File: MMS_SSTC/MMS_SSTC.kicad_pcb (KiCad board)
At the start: 2 copper layers, 80 x 80 mm, 39 parts, among them J1 Screw_Terminal_01x02, J2 Screw_Terminal_01x02, Q1 FQA8N100C, U1 NE555P, U2 UCC37322P, U3 LM7812_TO220, U4 LM7805_TO220, Y1 CXO_DIP8

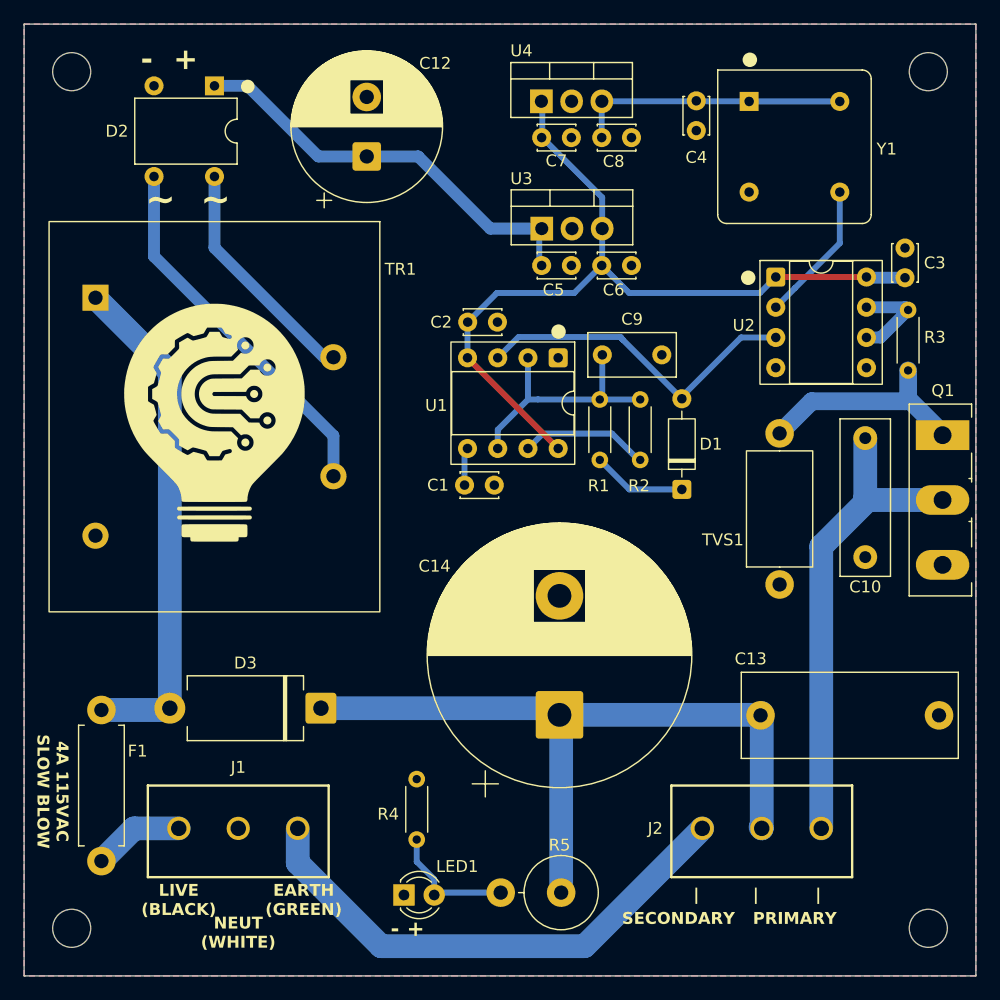
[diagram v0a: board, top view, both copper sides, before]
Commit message: Update PCB trace clearances
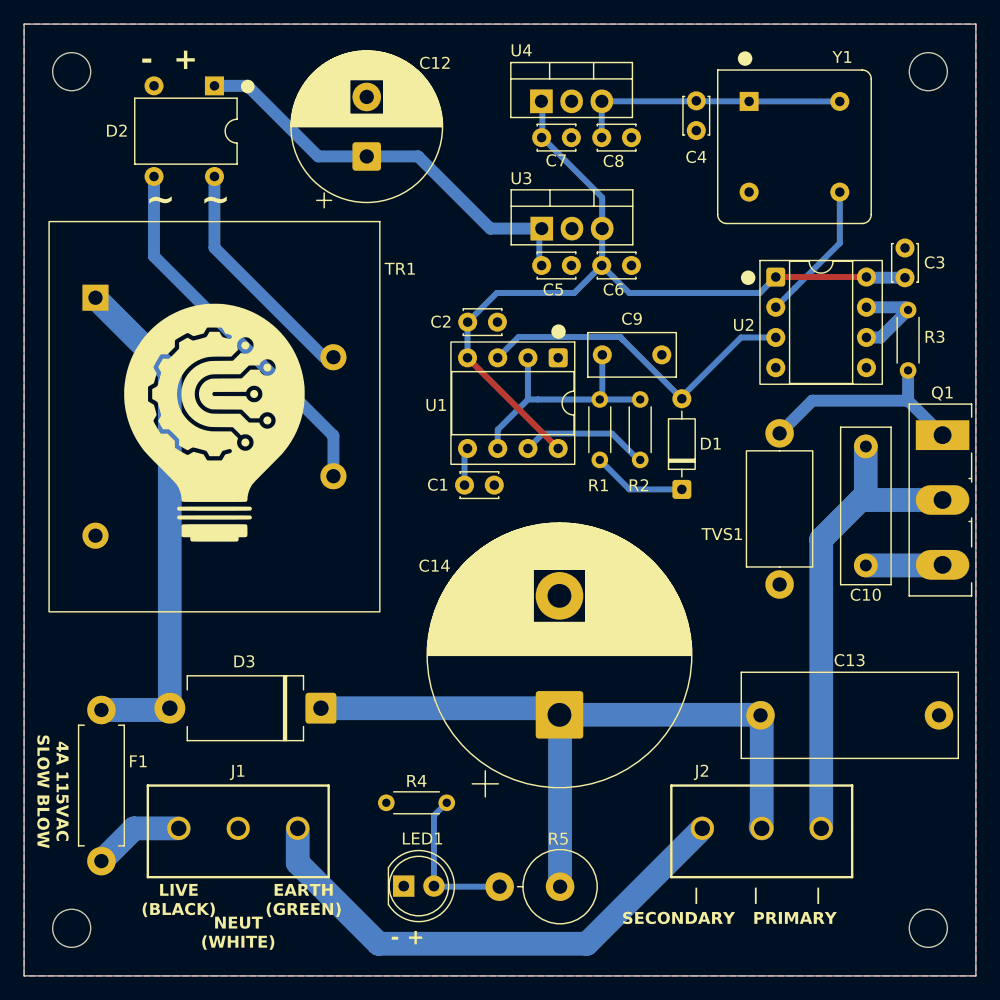
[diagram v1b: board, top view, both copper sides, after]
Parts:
- LED1: footprint LED_THT:LED_D3.0mm -> LED_THT:LED_D5.0mm
- moved R4 3.99 mm to (126.5, 130.4), turned to 180 degrees
- moved LED1 0.75 mm to (122.9, 137.4)
- moved C10 0.70 mm to (161.8, 100.5)
- moved R5 0.51 mm to (136.1, 137.5)
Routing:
- net GND: track 0.16 -> 6.63 mm
- net Net-(LED1-A): track 11.2 -> 13.3 mm

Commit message: Get CAD semi-finished, tweak PCB
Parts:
- moved TR1 1.25 mm to (117.0, 89.2)
- moved G*** 1.10 mm to (107.0, 99.6)
- renumbered C12 to C11, C13 to C12, C14 to C13
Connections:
- R5 pad 1: +170V -> unconnected-(R5-Pad1)
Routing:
- net GND: track 6.63 -> 10.9 mm
- net Net-(D2-Pad4): track 19.0 -> 20.6 mm
- net Net-(D2-Pad3): track 31.4 -> 32.7 mm
- net AC_PROT: track 43.3 -> 42.0 mm
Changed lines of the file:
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@@
 		(capping no)
 		(filling no)
-		(zone_defaults)
+		(grid_origin 91 145)
 		(pcbplotparams
 			(layerselection 0x00000000_00000000_55555555_5755f5ff)
@@
 			)
 		)
-		(property "DKPN" "160-1603-ND"
+		(property "DKPN" "2007-BL-BBX1V4V-2-B02-ND"
 			(at 0 0 0)
 			(unlocked yes)
@@
 			)
 		)
-		(attr through_hole exclude_from_bom)
+		(attr through_hole)
 		(duplicate_pad_numbers_are_jumpers no)
 		(fp_line
@@
 	(footprint "locals:Transformer_Zettler_BV301S18028"
 		(layer "F.Cu")
-		(at 117 88 -90)
+		(at 117 89.25 -90)
 		(tags "transformer Zettler")
 		(property "Reference" "TR1"
@@
 			(layers "*.Cu" "*.Mask")
 			(remove_unused_layers no)
-			(net "+170V")
+			(net "unconnected-(R5-Pad1)")
 			(pintype "passive")
 		)
@@
 		(descr "CP, Radial series, Radial, pin pitch=5.00mm, diameter=12.5mm, height=20mm, Electrolytic Capacitor")
 		(tags "CP Radial series Radial pin pitch 5.00mm diameter 12.5mm height 20mm Electrolytic Capacitor")
-		(property "Reference" "C12"
+		(property "Reference" "C11"
 			(at 7.823959 5.75 180)
 			(layer "F.SilkS")
@@
 		(descr "C, Rect series, Radial, pin pitch=15.00mm, length*width=18*7mm^2, Capacitor, http://www.wima.com/EN/WIMA_FKS_3.pdf")
 		(tags "C Rect series Radial pin pitch 15.00mm length 18mm width 7mm Capacitor")
-		(property "Reference" "C13"
+		(property "Reference" "C12"
 			(at 7.5 -4.6 0)
 			(layer "F.SilkS")
@@
 		(descr "CP, Radial series, Radial, pin pitch=10.00mm, diameter=22mm, height=40mm, Electrolytic Capacitor, http://www.vishay.com/docs/28342/058059pll-si.pdf")
 		(tags "CP Radial series Radial pin pitch 10.00mm diameter 22mm height 40mm Electrolytic Capacitor")
-		(property "Reference" "C14"
+		(property "Reference" "C13"
 			(at 12.5 -10.5 180)
 			(layer "F.SilkS")
@@
 	(footprint "LOGO"
 		(layer "F.Cu")
-		(at 107 98.5)
+		(at 107 99.6)
 		(property "Reference" "G***"
 			(at 0 0 0)
@@
 		)
 	)
+	(point
+		(at 91 145)
+		(size 1)
+		(layer "B.Cu")
+	)
 	(segment
 		(start 165.3 96.65)
@@
 	)
 	(segment
+		(start 168.15 110.5)
+		(end 168.2 110.45)
+		(width 2)
+		(layer "F.Cu")
+		(net "GND")
+	)
+	(segment
+		(start 168.2 110.45)
+		(end 165.6 110.45)
+		(width 2)
+		(layer "F.Cu")
+		(net "GND")
+	)
+	(segment
+		(start 161.75 110.5)
+		(end 163.4 110.5)
+		(width 2)
+		(layer "F.Cu")
+		(net "GND")
+	)
+	(segment
 		(start 137.06 71.53)
 		(end 137.02 71.49)
@@
 	)
 	(segment
-		(start 161.75 110.5)
-		(end 168.15 110.5)
+		(start 161.8 110.45)
+		(end 161.75 110.5)
 		(width 2)
 		(layer "B.Cu")
@@
 	)
 	(segment
-		(start 168.15 110.5)
-		(end 168.2 110.45)
+		(start 168.2 110.45)
+		(end 161.8 110.45)
 		(width 2)
 		(layer "B.Cu")
@@
 	)
 	(segment
-		(start 103.25 94.25)
-		(end 97 88)
+		(start 103.25 122.5)
+		(end 103.25 95.5)
+		(width 2)
+		(layer "B.Cu")
+		(net "AC_PROT")
+	)
+	(segment
+		(start 103.25 95.5)
+		(end 97 89.25)
 		(width 2)
 		(layer "B.Cu")
@@
 	)
 	(segment
-		(start 103.25 122.5)
-		(end 103.25 94.25)
-		(width 2)
-		(layer "B.Cu")
-		(net "AC_PROT")
-	)
-	(segment
-		(start 107 83.8)
-		(end 107 77.81)
+		(start 107 77.81)
+		(end 107 84.25)
 		(width 1)
 		(layer "B.Cu")
@@
 	)
 	(segment
-		(start 116.2 93)
-		(end 107 83.8)
+		(start 107 84.25)
+		(end 117 94.25)
 		(width 1)
 		(layer "B.Cu")
@@
 	)
 	(segment
-		(start 101.92 84.52)
-		(end 101.92 77.81)
+		(start 101.92 77.81)
+		(end 101.92 84.72)
 		(width 1)
 		(layer "B.Cu")
@@
 	)
 	(segment
-		(start 101.92 84.52)
-		(end 117 99.6)
+		(start 101.92 84.72)
+		(end 117 99.8)
 		(width 1)
 		(layer "B.Cu")
@@
 	)
 	(segment
-		(start 117 99.6)
-		(end 117 103)
+		(start 117 99.8)
+		(end 117 104.25)
 		(width 1)
 		(layer "B.Cu")
